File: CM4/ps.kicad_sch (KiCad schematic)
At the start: 9 parts, among them J1 USB_B, J10 TP4056, J2 Conn_01x02

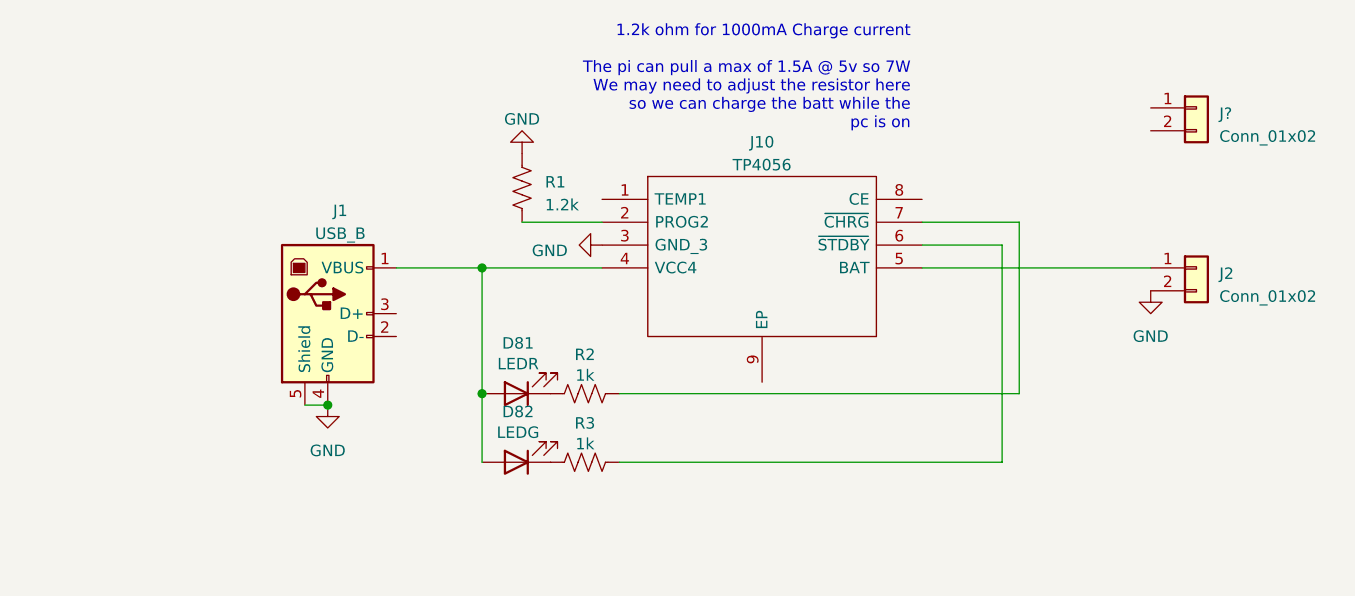
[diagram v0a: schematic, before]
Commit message: Working on adding new charge controller
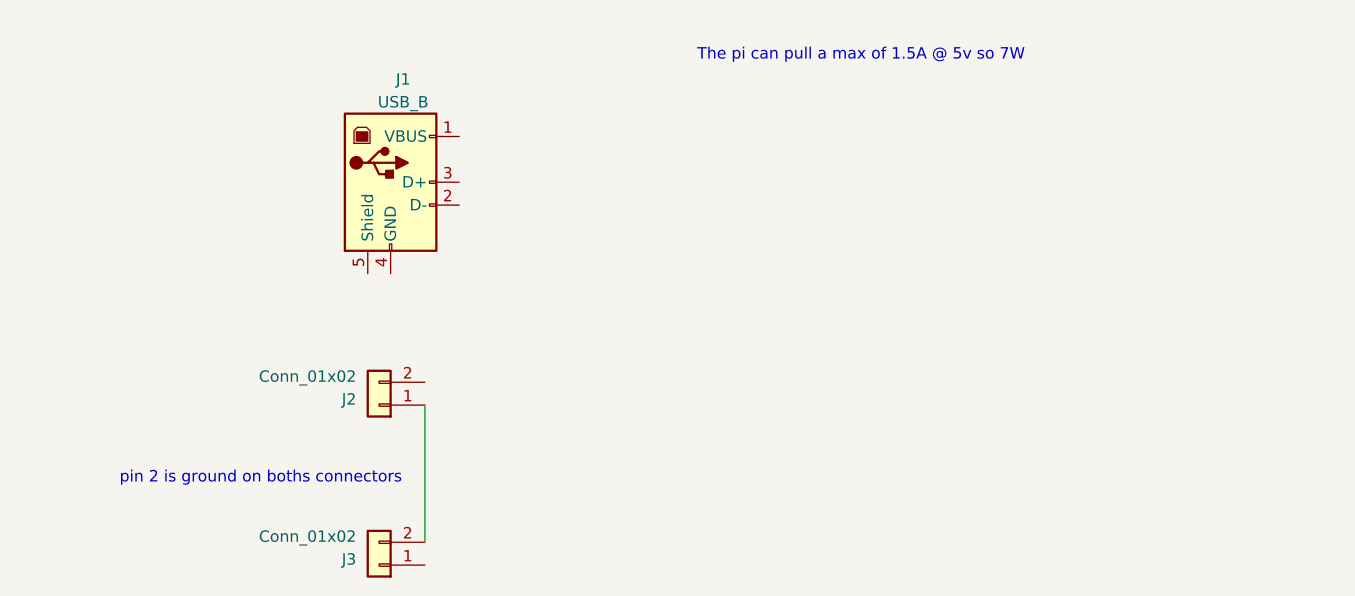
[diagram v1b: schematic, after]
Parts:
- removed D81: LEDR, LED_SMD:LED_1206_3216Metric, symbol Device:LED
- removed D82: LEDG, LED_SMD:LED_1206_3216Metric, symbol Device:LED
- removed J10: TP4056, teensy:SOIC127P600X175-9N, symbol tp4056:TP4056
- removed R1: 1.2k, Resistor_SMD:R_2010_5025Metric, symbol Device:R_US
- removed R2, R3: 1k, Resistor_SMD:R_2010_5025Metric, symbol Device:R_US
- gave numbers to parts that had none: 1
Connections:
- net at J2.1 (Pin_1): now also J3.2 (Pin_2)
- removed net GND: J1.4 (GND), J1.5 (Shield), J2.2 (Pin_2)
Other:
- note added: "The pi can pull a max of 1.5A @ 5v so 7W"
- note added: "pin 2 is ground on boths connectors"
- note removed: "1.2k ohm for 1000mA Charge current The pi can pull a max of 1.5A @ 5v so 7W We may need to adjust the resistor here so we can charge the batt while the pc is on"
- moved on the sheet: J1, J2, J3

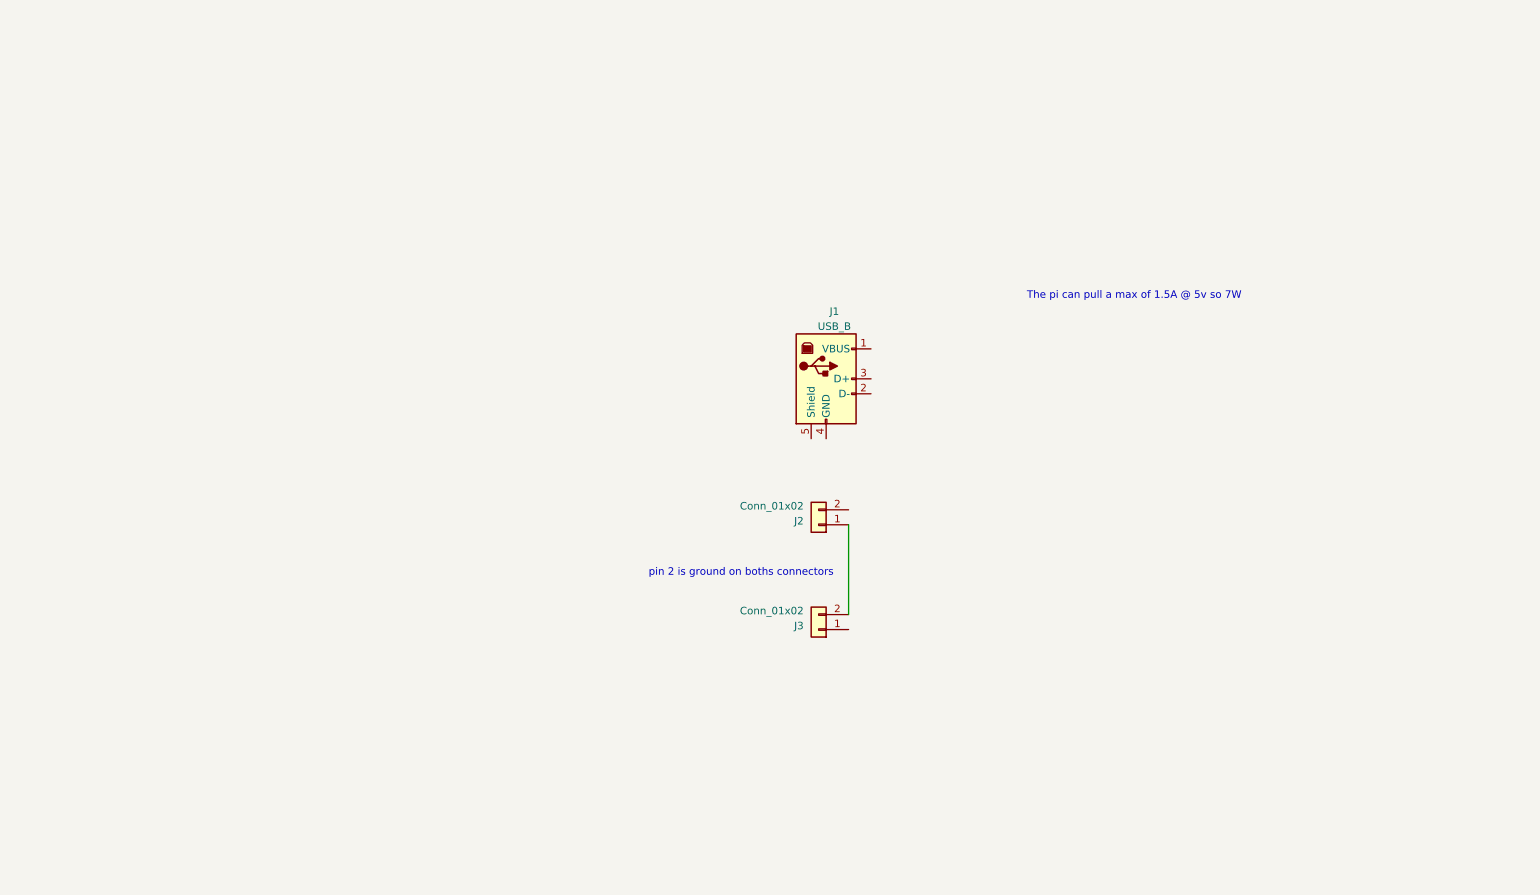
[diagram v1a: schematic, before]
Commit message: BatteryCharging COMPLEATE
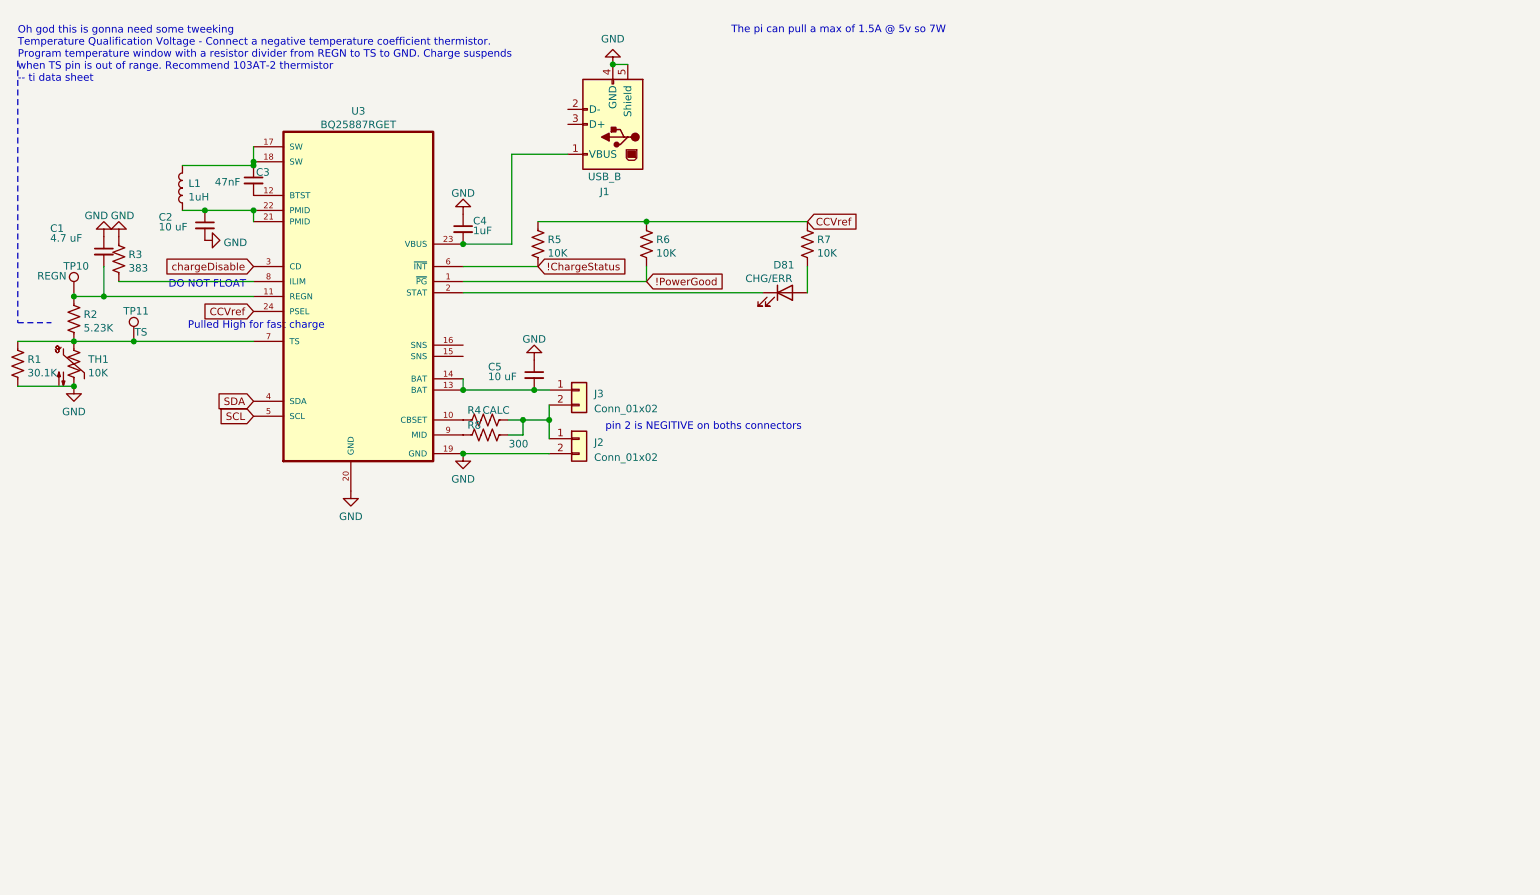
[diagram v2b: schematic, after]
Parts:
- added C1: 4.7 uF, Capacitor_SMD:C_1206_3216Metric, symbol Device:C_Small
- added C2, C5: 10 uF, Capacitor_SMD:C_1206_3216Metric, symbol Device:C_Small
- added C3: 47nF, Capacitor_SMD:C_1206_3216Metric, symbol Device:C_Small
- added C4: 1uF, Capacitor_SMD:C_1206_3216Metric, symbol Device:C_Small
- added D81: CHG/ERR, LED_SMD:LED_2010_5025Metric, symbol Device:LED
- added L1: 1uH, Inductor_SMD:L_1812_4532Metric, symbol Device:L
- added R1: 30.1K, Resistor_SMD:R_1206_3216Metric, symbol Device:R_US
- added R2: 5.23K, Resistor_SMD:R_1206_3216Metric, symbol Device:R_US
- added R3: 383, Resistor_SMD:R_1206_3216Metric, symbol Device:R_US
- added R4: CALC, Resistor_SMD:R_1206_3216Metric, symbol Device:R_US
- added R5, R6, R7: 10K, Resistor_SMD:R_1206_3216Metric, symbol Device:R_US
- added R8: 300, Resistor_SMD:R_1206_3216Metric, symbol Device:R_US
- added TH1: 10K, Connector_PinSocket_2.54mm:PinSocket_1x02_P2.54mm_Vertical, symbol Device:Thermistor_NTC_US
- added TP10: REGN, TestPoint:TestPoint_Pad_1.0x1.0mm, symbol Connector:TestPoint
- added TP11: TS, TestPoint:TestPoint_Pad_1.0x1.0mm, symbol Connector:TestPoint
- added U3: BQ25887RGET, Package_DFN_QFN:VQFN-24-1EP_4x4mm_P0.5mm_EP2.45x2.45mm_ThermalVias, symbol BQ25887RGET:BQ25887RGET
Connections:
- net at J2.1 (Pin_1), J3.2 (Pin_2): now also R4.1, R8.1
- net GND: now reaches J2.2 (Pin_2)
- net GND: now also J1.4 (GND), J1.5 (Shield), C1.1, C2.2, C4.1, C5.1, R1.1, R3.1, TH1.2, U3.19 (GND), U3.20 (GND)
- net at J1.1 (VBUS): now also C4.2, U3.23 (VBUS)
- net at J3.1 (Pin_1): now also C5.2, U3.13 (BAT), U3.14 (BAT)
- new net: R3.2, U3.8 (ILIM)
- new net: R1.2, R2.1, TH1.1, TP11.1, U3.7 (TS)
- new net: C1.2, R2.2, TP10.1, U3.11 (REGN)
- new net: R4.2, U3.10 (CBSET)
- new net: C2.1, L1.1, U3.21 (PMID), U3.22 (PMID)
- new net: C3.1, L1.2, U3.17 (SW), U3.18 (SW)
- new net: C3.2, U3.12 (BTST)
- new net: D81.1 (K), U3.2 (STAT)
- new net: R8.2, U3.9 (MID)
- new net: D81.2 (A), R7.1
- new net !ChargeStatus: R5.1, U3.6 (~INT)
- new net !PowerGood: R6.1, U3.1 (~PG)
- new net CCVref: R5.2, R6.2, R7.2, U3.24 (PSEL)
- new net SCL: U3.5 (SCL)
- new net SDA: U3.4 (SDA)
- new net chargeDisable: U3.3 (CD)
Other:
- note added: "DO NOT FLOAT"
- note added: "Oh god this is gonna need some tweeking Temperature Qualification Voltage - Connect a negative temperature coefficient thermistor. Program temperature window with a resistor divider from REGN to TS to GND. Charge suspends when TS pin is out of range. Recommend 103AT-2 thermistor -- ti data sheet"
- note added: "Pulled High for fast charge"
- note added: "pin 2 is NEGITIVE on boths connectors"
- note removed: "pin 2 is ground on boths connectors"
- moved on the sheet: J1, J2, J3

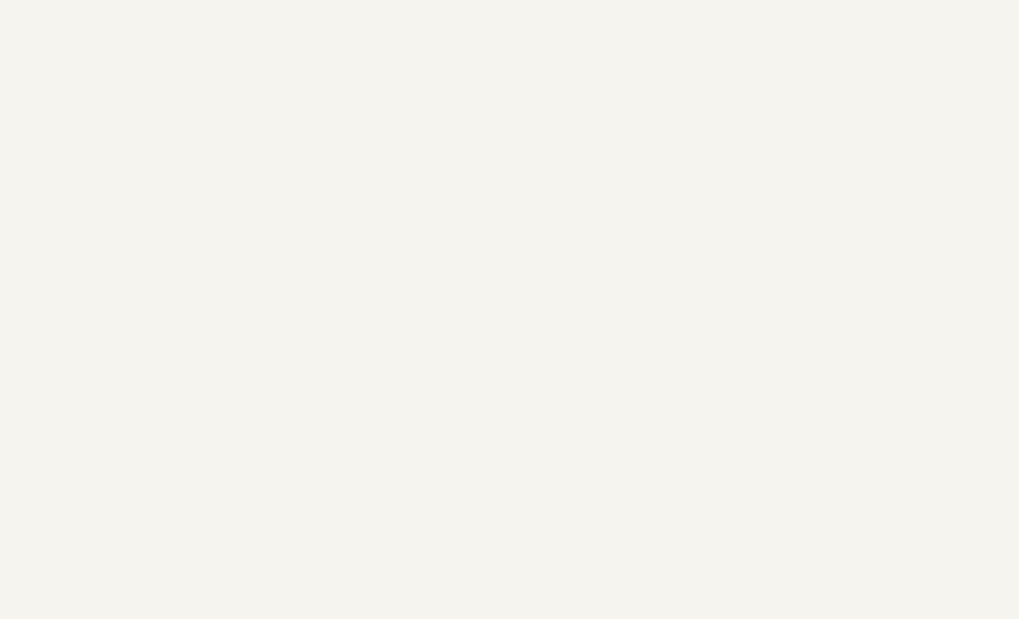
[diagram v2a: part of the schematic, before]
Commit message: Laid out 5v ic and battery charger
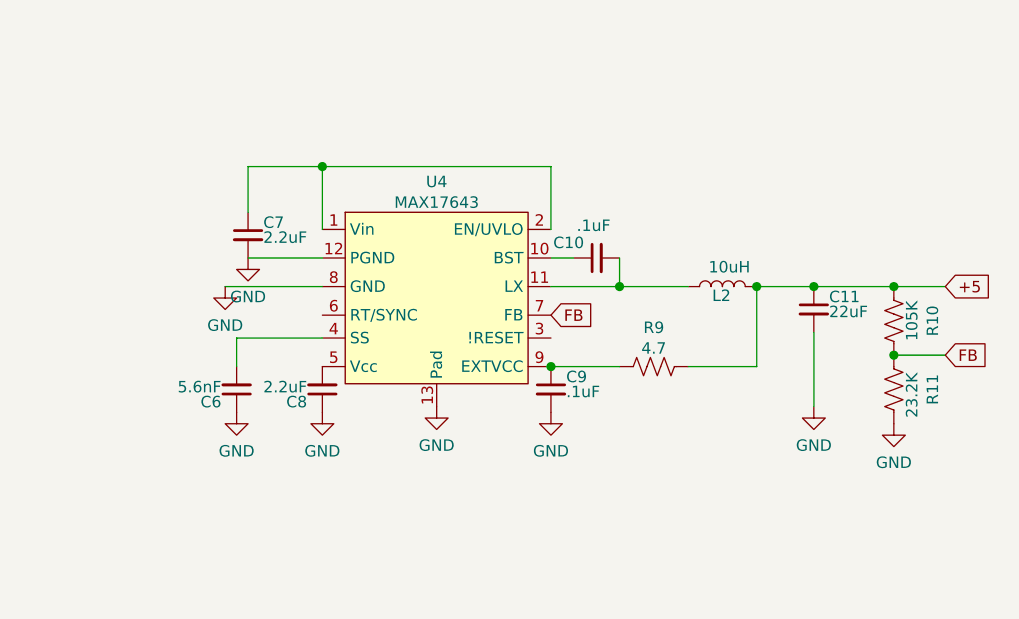
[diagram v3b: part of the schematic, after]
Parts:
- added C10, C9: .1uF, Capacitor_SMD:C_1206_3216Metric, symbol Device:C_Small
- added C11: 22uF, Capacitor_SMD:C_1206_3216Metric, symbol Device:C_Small
- added C6: 5.6nF, Capacitor_SMD:C_1206_3216Metric, symbol Device:C_Small
- added C7, C8: 2.2uF, Capacitor_SMD:C_1206_3216Metric, symbol Device:C_Small
- added L2: 10uH, Inductor_SMD:L_1812_4532Metric, symbol Device:L
- added R10: 105K, Resistor_SMD:R_1206_3216Metric, symbol Device:R_US
- added R11: 23.2K, Resistor_SMD:R_1206_3216Metric, symbol Device:R_US
- added R9: 4.7, Resistor_SMD:R_1206_3216Metric, symbol Device:R_US
- added U4: MAX17643, trinamic-footprints:TDFN-12_3x3mm_P0.5mm, symbol teensy:MAX17643
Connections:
- net GND: now also C11.2, C6.1, C7.2, C8.1, C9.2, R11.2, U4.12 (PGND), U4.13 (Pad), U4.8 (GND)
- new net: C9.1, R9.1, U4.9 (EXTVCC)
- new net: C7.1, U4.1 (Vin), U4.2 (EN/UVLO)
- new net: C10.1, U4.10 (BST)
- new net: C10.2, L2.1, U4.11 (LX)
- new net: C6.2, U4.4 (SS)
- new net: C8.2, U4.5 (Vcc)
- new net +5: C11.1, L2.2, R10.1, R9.2
- new net FB: R10.2, R11.1, U4.7 (FB)
